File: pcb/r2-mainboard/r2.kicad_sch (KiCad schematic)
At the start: 0 parts

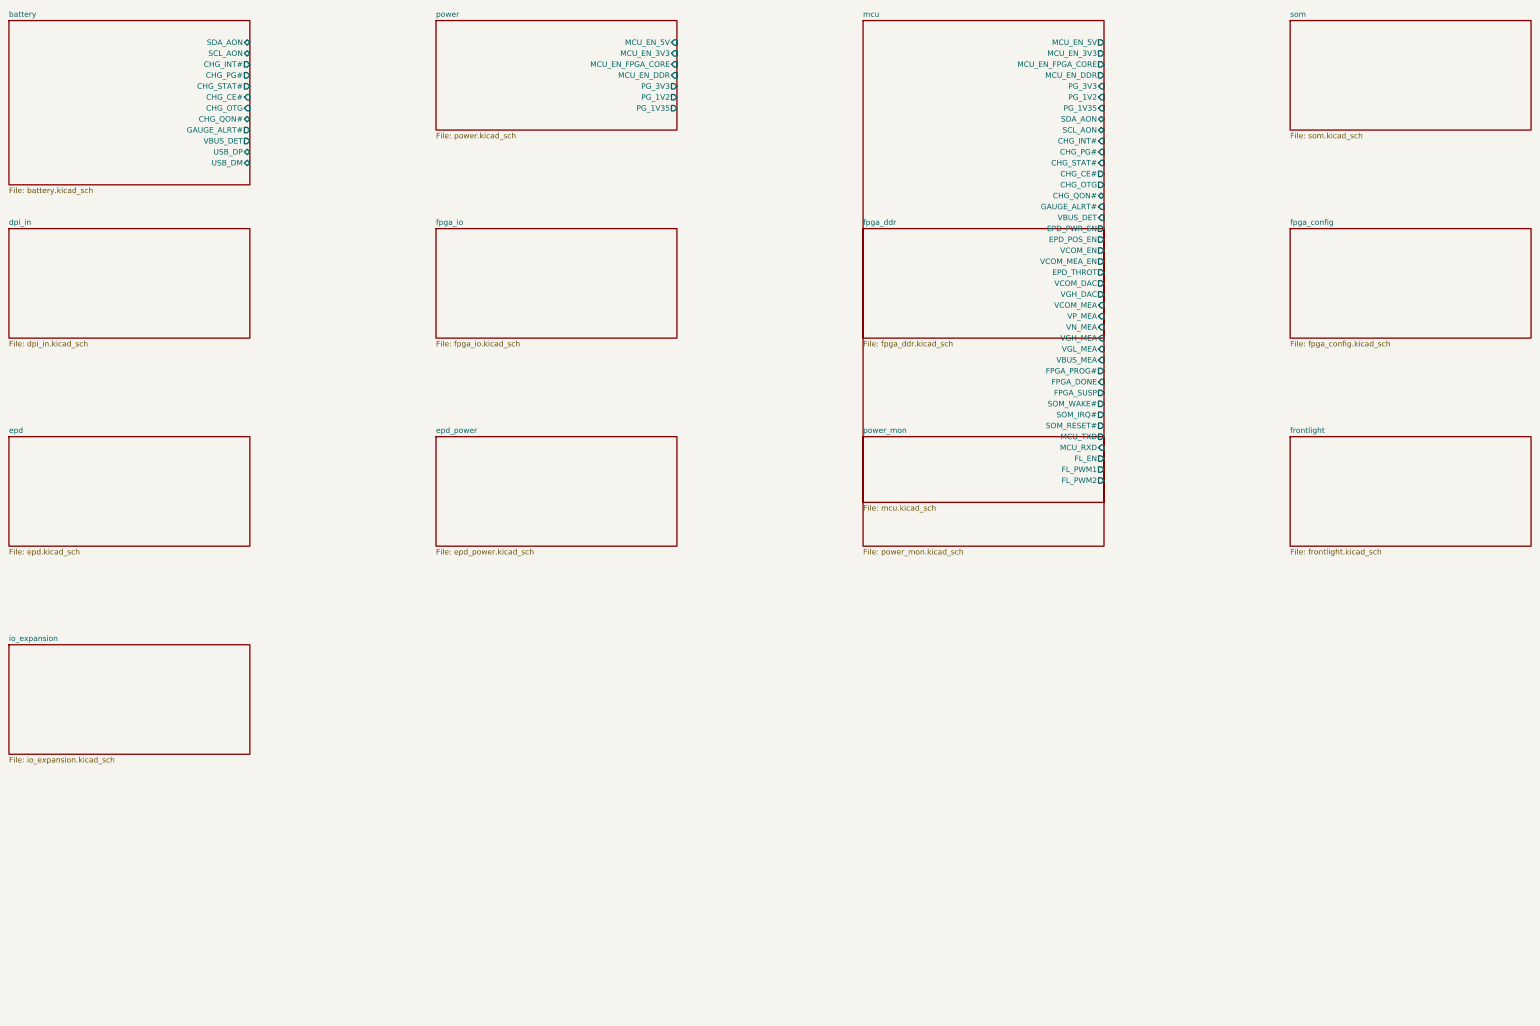
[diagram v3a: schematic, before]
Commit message: R2: port epd, epd_power and power_mon from R1
WP4. These three sheets are copied from pcb/mainboard/ rather than redrawn,
because the acceptance criterion is "is it the same as R1" -- copying keeps
every part, value, coordinate and wire, so the two can be diffed directly.
tools/port_r1.py does it and only ever reads R1.

Result: epd and epd_power are provably identical to R1. R1's netlist was
exported from a scratch copy and the partition of each sheet's pins into nets
compared with R2's, undoing the designator renames first: 49/49 and 44/44 net
groups, identical. power_mon differs in exactly four groups, all intended.

103 of 128 parts keep their exact R1 designator; only collisions are renamed,
+200 for R/C and +20 for U/L so the R1 number stays readable inside the new one.
Other transforms: global labels become hierarchical labels (they are different
nets in KiCad, so a mixed project would have failed to connect silently);
I2C1_* becomes *_AON; three transistor symbols moved library in KiCad 10;
SY8120 and MT9700 are lifted into r2.kicad_sym because they are not in
pcb_common at all -- in R1 they survive only as embedded definitions.

power_mon's two video-decoder channels are gone with the ADV7611, so three
shunts are repurposed without any topology change: U22 now measures the SoM's
input current, the always-on domain, and the frontlight from +VSYS. All three
INA3221s move to +3V3_AON -- on a switched rail their I2C pins would clamp the
always-on bus, and power-down IQ is 0.5 uA typ, so the always-on domain finally
becomes measurable.

Two open items closed by reading R1 properly:

- The EPD chain cannot run from +VSYS. LGS5145 is a buck with a 4.5 V minimum,
  used here as an inverting buck-boost; in steady state it sees ~25 V, but at
  startup the negative rail is at 0 V and 3.0 V from a flat cell will not start
  it. power.md §9 closed.
- Negative rails are measured by dividing between the rail and +3V3_DCDC, not
  to ground. Carried over unchanged, with a f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
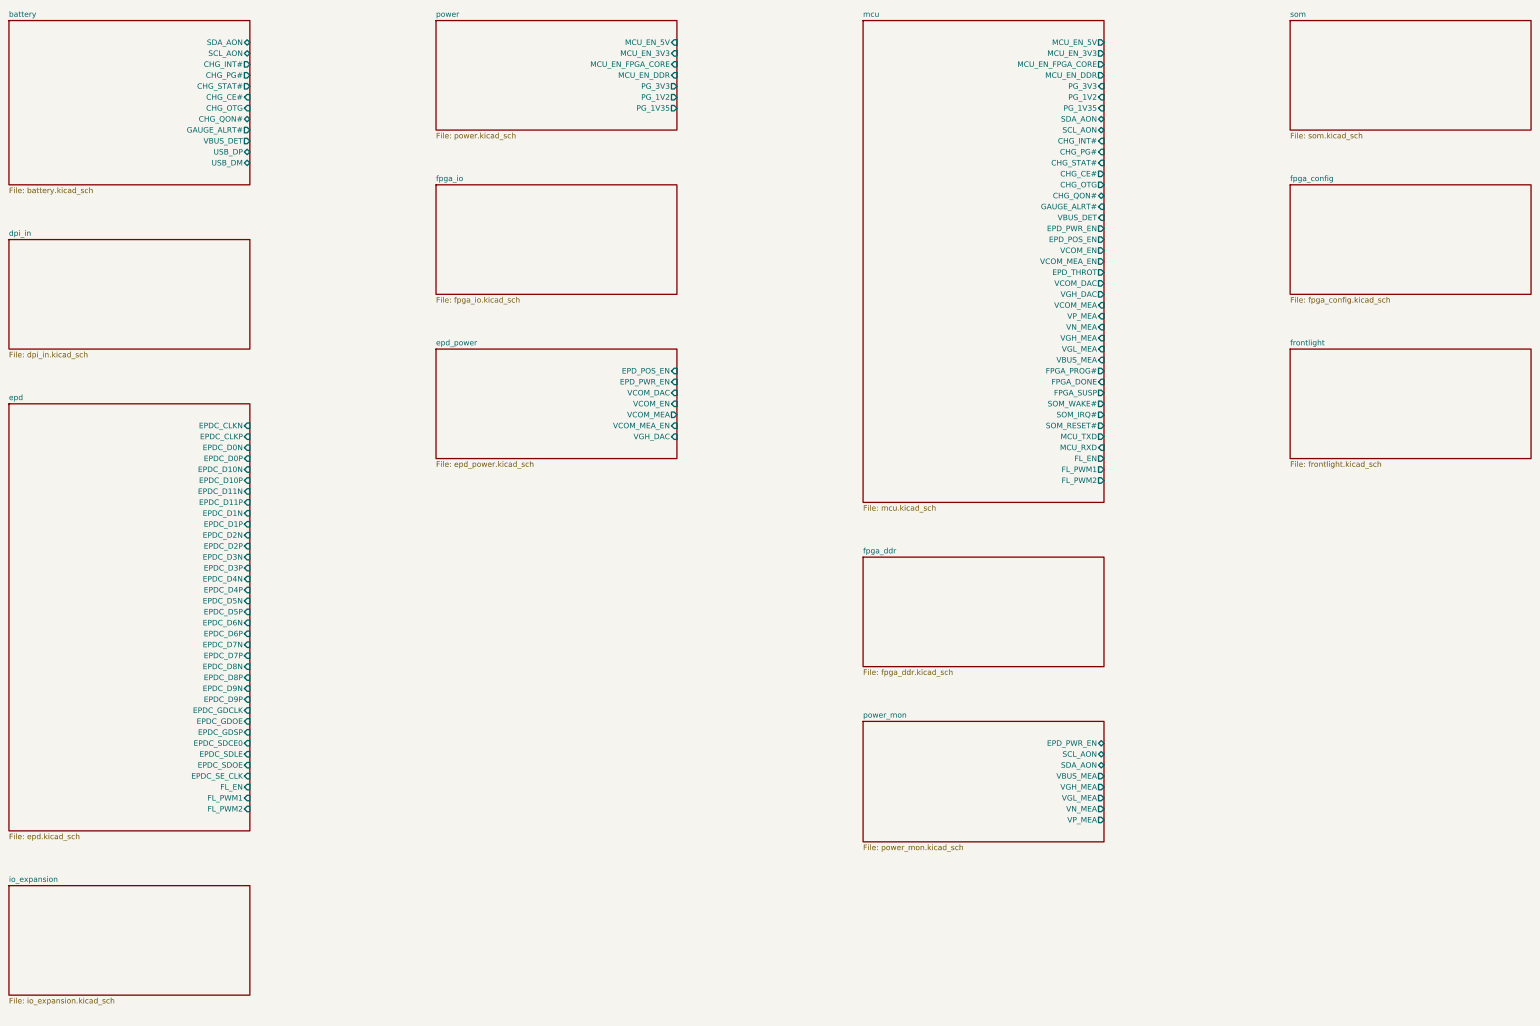
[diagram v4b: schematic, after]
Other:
- sheet epd ports: added EPDC_CLKN, EPDC_CLKP, EPDC_D0N, EPDC_D0P, EPDC_D10N, EPDC_D10P, EPDC_D11N, EPDC_D11P, EPDC_D1N, EPDC_D1P, EPDC_D2N, EPDC_D2P, EPDC_D3N, EPDC_D3P, EPDC_D4N, EPDC_D4P, EPDC_D5N, EPDC_D5P, EPDC_D6N, EPDC_D6P, EPDC_D7N, EPDC_D7P, EPDC_D8N, EPDC_D8P, EPDC_D9N, EPDC_D9P, EPDC_GDCLK, EPDC_GDOE, EPDC_GDSP, EPDC_SDCE0, EPDC_SDLE, EPDC_SDOE, EPDC_SE_CLK, FL_EN, FL_PWM1, FL_PWM2; removed none
- sheet epd_power ports: added EPD_POS_EN, EPD_PWR_EN, VCOM_DAC, VCOM_EN, VCOM_MEA, VCOM_MEA_EN, VGH_DAC; removed none
- sheet power_mon ports: added EPD_PWR_EN, SCL_AON, SDA_AON, VBUS_MEA, VGH_MEA, VGL_MEA, VN_MEA, VP_MEA; removed none

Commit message: R2: WP5 groundwork -- Xilinx/Micron datasheets, LX16 fix, DDR bank to 1.5 V
Steps 1-3 of the WP5 plan. No FPGA sheet is drawn yet; this is the evidence base
and the one power change that had to land before fpga_ddr can be.

DATASHEETS
AMD's documentation portal no longer serves PDFs at any of the old xilinx.com
paths -- every URL returns the same 2.5 KB JavaScript shell -- so these came from
the Wayback Machine: ds162 (DC & Switching), ug380 (Configuration), ug381
(SelectIO), ug393 (PCB Design). The hardware owner supplied mt41k64m16 from
DigiKey after micron.com proved unreachable. UG385 Packaging was deliberately
skipped at 15.8 MB, since pcb_common's XC6SLX-FTG256 symbol already encodes bank
membership in its pin names.

THE FPGA IS AN LX16, NOT AN LX9
NOTES-R2-plan.md's architecture diagram said XC6SLX9 and
NOTES-R2-hardware-facts.md carried a BOM row for XC6SLX9-2FTG256C at $6.10 --
stock and price for the wrong device. The gateware targets xc6slx16-ftg256-3 in
four places (caster.xise Device/Package/Speed Grade, par/ise_flow.sh,
par/ise_run.txt, mig.prj TargetFPGA) and R1's own schematic says
XC6SLX16-FTG256. An LX9 is not a drop-in: the MIG's C3_SMALL_DEVICE parameter
exists specifically for xc6slx9 packages, so it would need the memory controller
regenerated. LCSC stock and price for the LX16 are marked for re-query rather
than guessed.

DDR BANK 1.35 V -> 1.5 V
Caster's UCF constrains all 48 DDR pins as SSTL15_II / DIFF_SSTL15_II /
LVCMOS15, and ds162.pdf Table 7 specifies SSTL15_II only over VCCO
1.425-1.575 V with VREF 0.69-0.81 V. The committed rail was 1.344 V -- 81 mV
below the VCCO minimum, with a half-rail VREF of 0.672 V below its minimum too.
Spartan-6 has no 1.35 V I/O standard to relabel the gateware to: SSTL135 appears
nowhere in ds162.pdf or ug381.pdf, and LVCMOS15 and the HSTL standards still
stop at 1.4 V. R1 runs the same way and works, but on a different layout, and
neither board can be tested from here.

mt41k64m16.pdf p.1 makes the fix fr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
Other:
- sheet mcu ports: added PG_1V5; removed PG_1V35
- sheet power ports: added PG_1V5; removed PG_1V35
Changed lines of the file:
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@@
 			)
 		)
-		(pin "PG_1V35" output
+		(pin "PG_1V5" output
 			(at 177.8 50.8 0)
 			(effects
@@
 			)
 		)
-		(pin "PG_1V35" input
+		(pin "PG_1V5" input
 			(at 276.86 50.8 0)
 			(effects

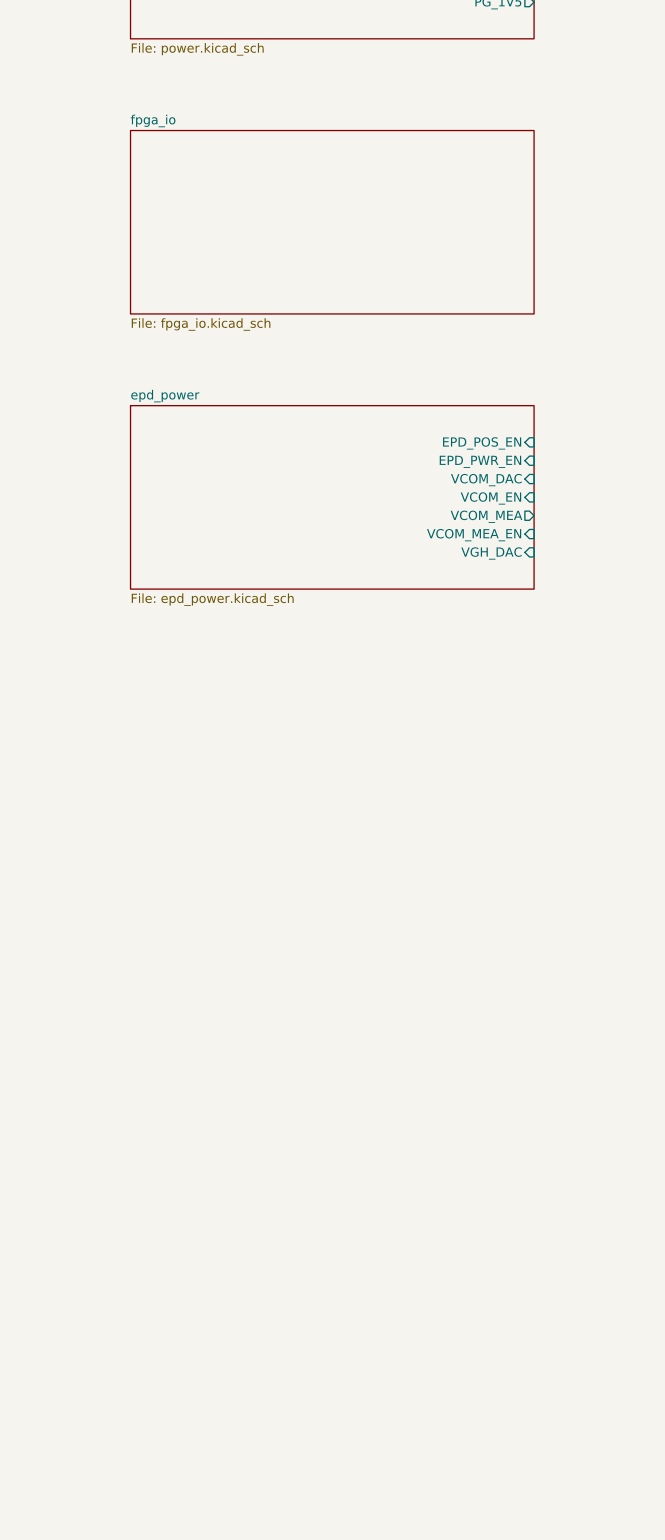
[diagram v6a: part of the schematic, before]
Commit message: R2: WP5 -- fpga_io ported, verified pin-for-pin against R1
Banks 0 and 1 of the XC6SLX16: the EPD panel bus out, DPI in. Ported from R1 by
an extended tools/port_r1.py rather than redrawn, so the pinout the gateware
depends on cannot drift -- Caster's constraint.ucf fixes almost all of it and
ISE 14.7 is the only toolchain that still targets Spartan-6.

RESULT
69 signal nets identical to R1, zero mismatches: every EPDC_*, DPI_*, LED,
EPD_THROT and VCCO ball lands on exactly the pin R1 used. All 33 EPDC_*
hierarchical labels on epd.kicad_sch have exactly one source here, no more and
no fewer. ERC on /fpga_io/ is 4, all of them "units C/D/E/F of U41 are not
placed yet" (missing_unit, missing_power_pin, missing_bidi_pin,
power_pin_not_driven) which resolve as fpga_ddr, fpga_config and unit 6 land.

THE 12 FMC SIGNALS ARE DELETED
R1 wires a 12-signal parallel bus between the H750's FMC and the FPGA --
FMC_A16, FMC_D0-D7, FMC_NE1, FMC_NOE, FMC_NWE -- but no .ucf in Caster assigns
any of it, so the gateware has never used that bus. R2 has no MCU-side parallel
bus at all. The labels and their stubs go and the freed bank-1 pins get
no-connect flags.

A CROSS-SHEET SHORT, CAUGHT ONLY BY THE PIN-MAP CHECK
The first run reported 7 mismatches: U41.D14 on VCOM_MEA_EN, J14 on SHDN, and
five more. Adding 57 sheet pins grew fpga_io's box on the root to y 68.6-221.0
and epd_power was sitting at y 106.7-132.1 in the same column, so their sheet
pins overlapped and the nets shorted. This is the hazard docs/epd-port.md §8
records; tools/layout_root.py moved epd_power to y 233.68 and the check now
asserts no two sheet boxes on the root overlap.

Worth recording because it is the argument for the check: ERC did not catch
this, and neither did anything else. Only comparing every ball against R1 did.
tools/check_ucf.py should exist before fpga_ddr, where one swapped MCB3 pin is
fatal and invisible.

R1 LEAVES 12 OF ITS 24 SPARE BALLS UNFLAGGED
Those arrived as pin_not_connected. docs/mcu.md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
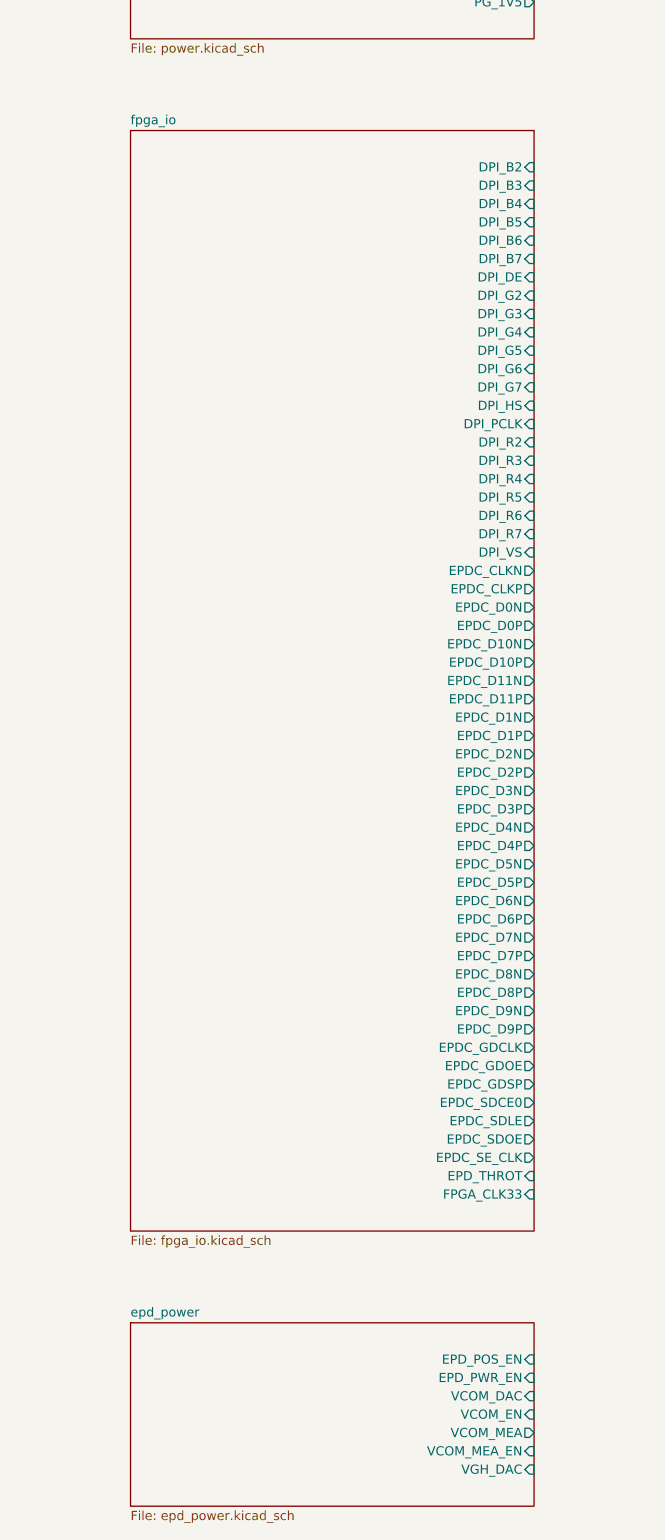
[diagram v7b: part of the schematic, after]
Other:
- sheet fpga_io ports: added DPI_B2, DPI_B3, DPI_B4, DPI_B5, DPI_B6, DPI_B7, DPI_DE, DPI_G2, DPI_G3, DPI_G4, DPI_G5, DPI_G6, DPI_G7, DPI_HS, DPI_PCLK, DPI_R2, DPI_R3, DPI_R4, DPI_R5, DPI_R6, DPI_R7, DPI_VS, EPDC_CLKN, EPDC_CLKP, EPDC_D0N, EPDC_D0P, EPDC_D10N, EPDC_D10P, EPDC_D11N, EPDC_D11P, EPDC_D1N, EPDC_D1P, EPDC_D2N, EPDC_D2P, EPDC_D3N, EPDC_D3P, EPDC_D4N, EPDC_D4P, EPDC_D5N, EPDC_D5P, EPDC_D6N, EPDC_D6P, EPDC_D7N, EPDC_D7P, EPDC_D8N, EPDC_D8P, EPDC_D9N, EPDC_D9P, EPDC_GDCLK, EPDC_GDOE, EPDC_GDSP, EPDC_SDCE0, EPDC_SDLE, EPDC_SDOE, EPDC_SE_CLK, EPD_THROT, FPGA_CLK33; removed none
